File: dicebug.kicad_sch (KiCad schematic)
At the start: 33 parts, among them SW1 SW_SPDT, U1 74LV163ADR, U3 74HCS7266DR, U5 iqs211a

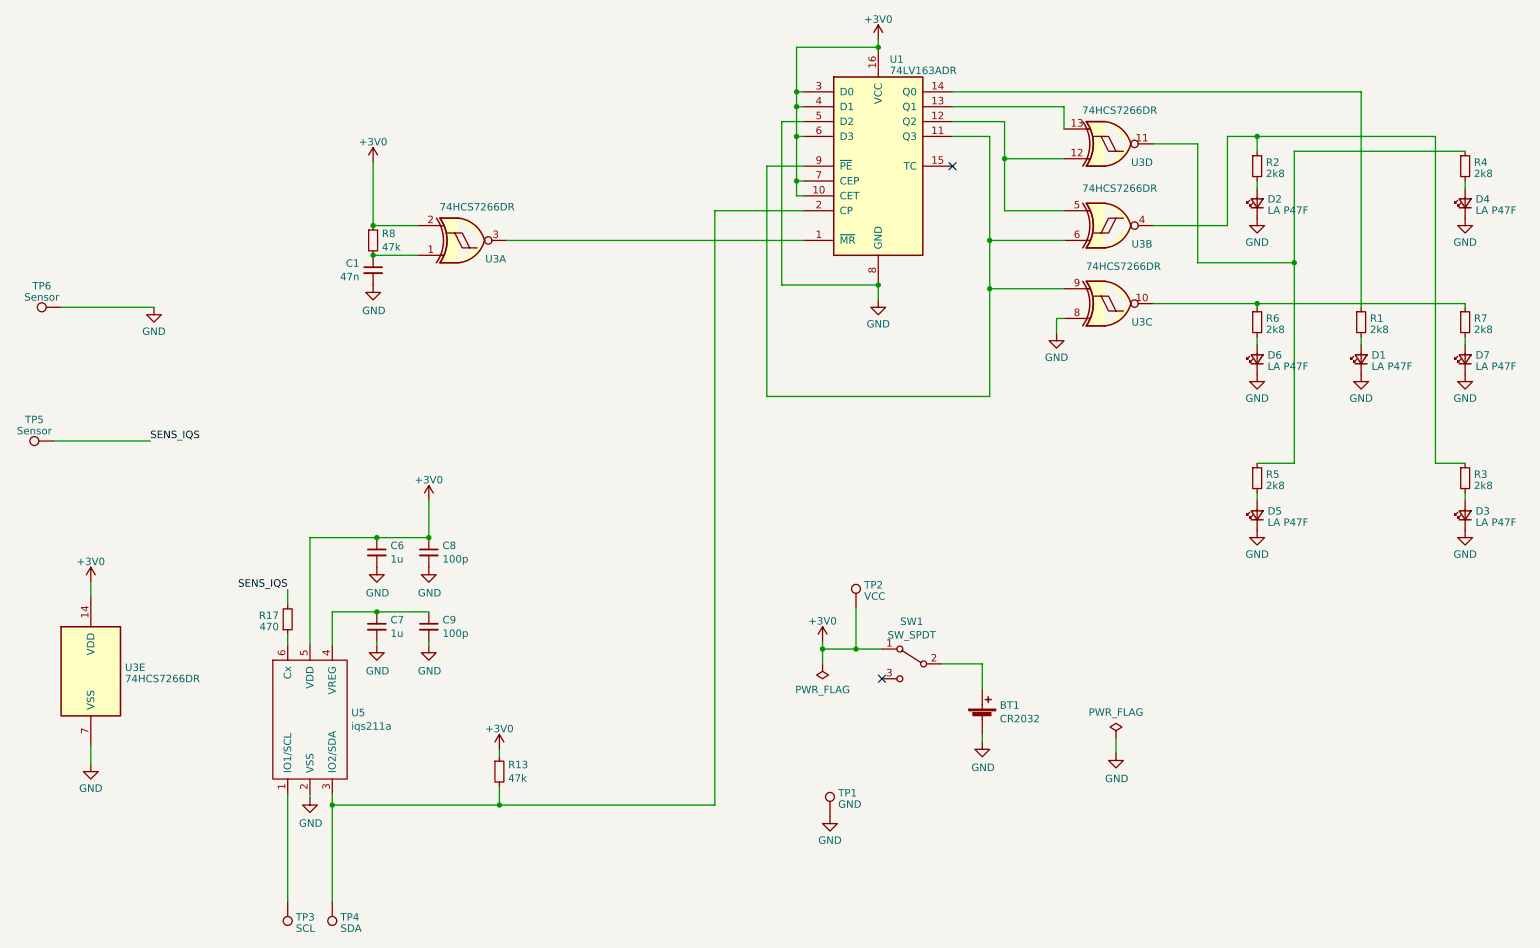
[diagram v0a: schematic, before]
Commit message: updated part values, numbers/id and manufacturers; added comments
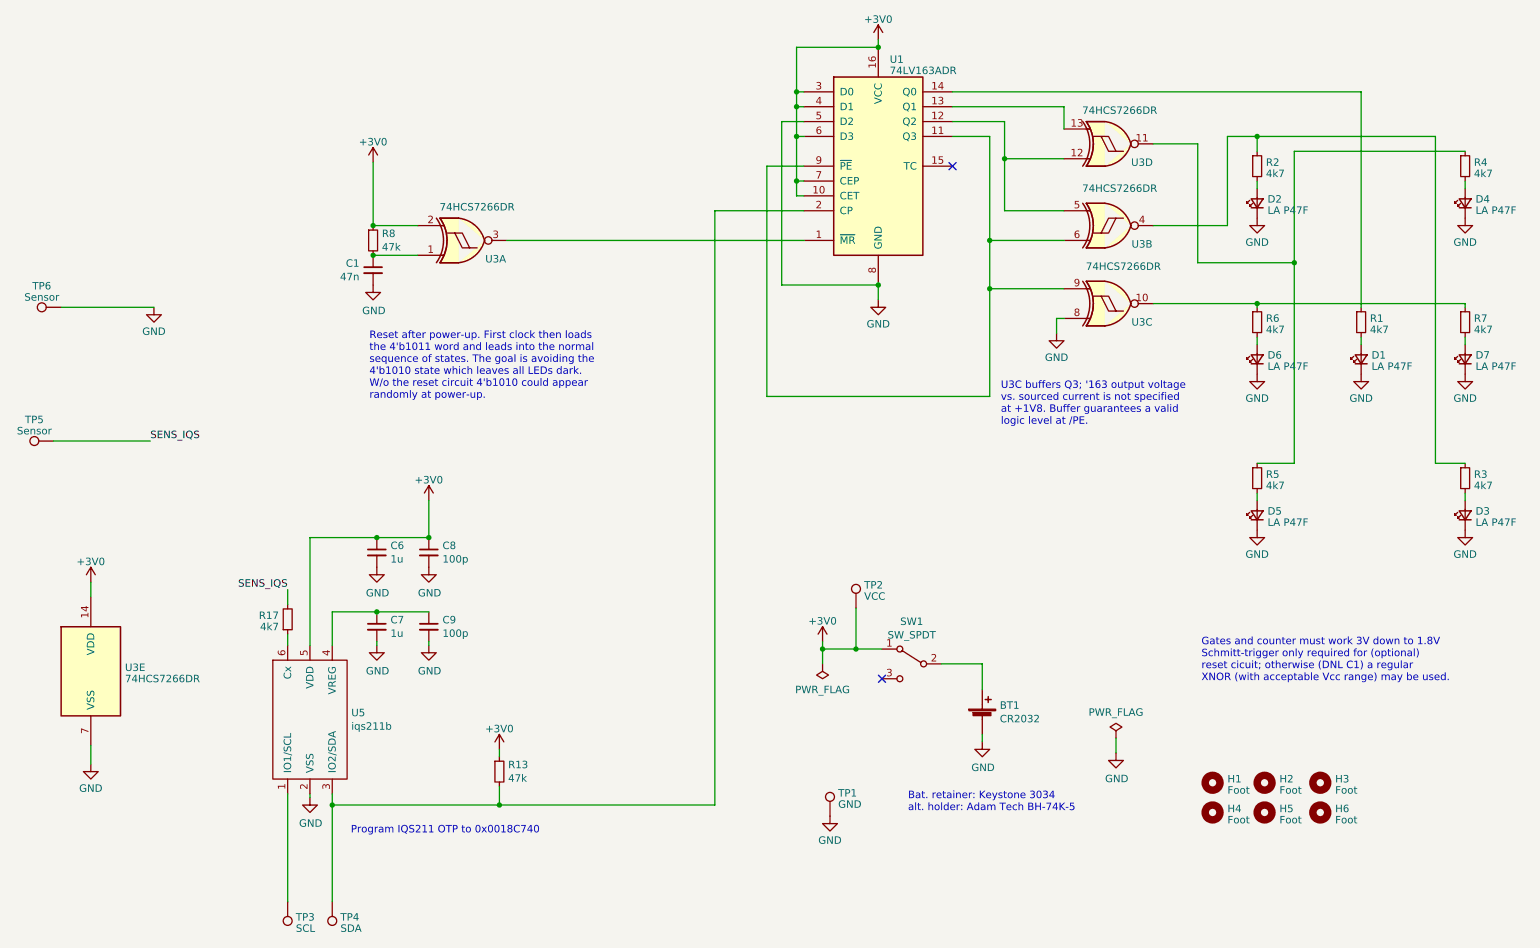
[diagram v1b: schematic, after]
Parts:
- added H1, H2, H3, H4, H5, H6: Foot, sensors:foot, symbol Mechanical:MountingHole
- BT1: Manufacturer Linx -> Keystone; Part BAT-HLD-012-SMT‎ -> 3034
- D1, D2, D3, D4, D5, D6, D7: Manufacturer (none) -> Osram; Part (none) -> LA P47F-V2BB-24-3A4B-Z
- R1, R2, R3, R4, R5, R6, R7: value 2k8 -> 4k7
- R17: value 470 -> 4k7
- U1: Part (none) -> 74LV163ADR
- U3: Part (none) -> 74HCS7266DR
- U5: value iqs211a -> iqs211b; Manufacturer (none) -> Azoteq; Part (none) -> IQS211B
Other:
- note added: "Bat. retainer: Keystone 3034 alt. holder: Adam Tech BH-74K-5"
- note added: "Gates and counter must work 3V down to 1.8V Schmitt-trigger only required for (optional) reset cicuit; otherwise (DNL C1) a regular XNOR (with acceptable Vcc range) may be used."
- note added: "Program IQS211 OTP to 0x0018C740"
- note added: "Reset after power-up. First clock then loads the 4'b1011 word and leads into the normal sequence of states. The goal is avoiding the 4'b1010 state which leaves all LEDs dark. W/o the reset circuit 4'b1010 could appear randomly at power-up."
- note added: "U3C buffers Q3; '163 output voltage vs. sourced current is not specified at +1V8. Buffer guarantees a valid logic level at /PE."

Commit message: Added title + author info to schematic
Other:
- company: (none) -> Till Straumann
- title: (none) -> DiceBug
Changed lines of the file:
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@@
 (kicad_sch (version 20230121) (generator eeschema)
   (paper "A4")
+  (title_block
+    (title "DiceBug")
+    (date "2023-05-30")
+    (rev "1.0")
+    (company "Till Straumann")
+  )
   (junction (at 231.14 71.755) (diameter 0) (color 0 0 0 0)
   )

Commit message: Fixed fab layer
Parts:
- C1: Manufacturer Kemet -> Samsung; Part C0603C101J5GACTU -> CL21B473KCFNNNF
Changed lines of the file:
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@@
       (effects (font (size 1.27 1.27)) hide)
     )
-    (property "Part" "C0603C101J5GACTU " (at 80.01 66.04 0)
+    (property "Part" "CL21B473KCFNNNF" (at 80.01 66.04 0)
       (effects (font (size 1.27 1.27)) hide)
     )
-    (property "Manufacturer" "Kemet" (at 80.01 66.04 0)
+    (property "Manufacturer" "Samsung" (at 80.01 66.04 0)
       (effects (font (size 1.27 1.27)) hide)
     )
